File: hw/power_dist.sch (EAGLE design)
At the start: 83 parts, among them J1 JST-ZH6SMT_VERT, J2 JST-PH4SMT_VERT, J3 JST-PH5VERT, P1 XT30P, P2 XT30P, P3 XT30P, P4 XT30P, P5 XT30P, P6 XT30P, P7 XT90PW-M, Q1 PSMN4R8-100BSEJ, Q2 PSMN4R8-100BSEJ, Q3 PSMN4R8-100BSEJ, Q4 MF-DSC-SOT233-MMBT3904, Q5 MMBT5401 100V, U1 MAX15062AATA+T, U2 STM32G474CEU6, U3 TPS2490DGSR, U4 TCAN334G, U5 LT1787HVIMS8PBF

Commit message: Connect TIMER to an ADC and add a FET temperature sensor
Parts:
- added C21: 0.1uF, mfpassives:CAPACITOR_NP_0603
- added U6: STLM20DD9FUDFN-4L_STM-L, power_dist:STLM20DD9FUDFN-4L_STM-L
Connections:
- new net FET_TEMP: U2.PC4, U6.VOUT
- net GND: now also C21.P$2, U6.GND
- net TIMER: now also U2.PB11
- net VCC: now also C21.P$1, U6.VCC
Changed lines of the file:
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@@
 </part>
 <part name="GND7" library="supply1" deviceset="GND" device=""/>
+<part name="U6" library="power_dist" deviceset="STLM20DD9F" device="UDFN-4L_STM-L">
+<attribute name="MPN" value="STLM20DD9F"/>
+<attribute name="POPULATE" value="1"/>
+</part>
+<part name="P+8" library="supply1" deviceset="VCC" device=""/>
+<part name="GND9" library="supply1" deviceset="GND" device=""/>
+<part name="C21" library="mfpassives" deviceset="CAPACITOR_NP" device="_0603" value="0.1uF">
+<attribute name="HOUSEPART" value="1"/>
+<attribute name="MPN" value="MF-CAP-0603-0.1uF"/>
+</part>
 </parts>
 <sheets>
@@
 <attribute name="VALUE" x="-38.1" y="5.08" size="1.778" layer="96"/>
 </instance>
+<instance part="U6" gate="A" x="134.62" y="-66.04" smashed="yes">
+<attribute name="NAME" x="150.2156" y="-56.9214" size="2.0828" layer="95" ratio="6" rot="SR0"/>
+<attribute name="VALUE" x="149.5806" y="-59.4614" size="2.0828" layer="96" ratio="6" rot="SR0"/>
+<attribute name="MPN" x="134.62" y="-66.04" size="1.778" layer="96" display="off"/>
+<attribute name="POPULATE" x="134.62" y="-66.04" size="1.778" layer="96" display="off"/>
+</instance>
+<instance part="P+8" gate="VCC" x="180.34" y="-45.72" smashed="yes">
+<attribute name="VALUE" x="177.8" y="-48.26" size="1.778" layer="96" rot="R90"/>
+</instance>
+<instance part="GND9" gate="1" x="180.34" y="-83.82" smashed="yes">
+<attribute name="VALUE" x="177.8" y="-86.36" size="1.778" layer="96"/>
+</instance>
+<instance part="C21" gate="G$1" x="180.34" y="-68.58" smashed="yes">
+<attribute name="NAME" x="182.88" y="-67.056" size="1.016" layer="95" font="vector" align="top-left"/>
+<attribute name="VALUE" x="182.88" y="-70.104" size="1.016" layer="96" font="vector"/>
+</instance>
 </instances>
 <busses>
@@
 <pinref part="GND7" gate="1" pin="GND"/>
 <wire x1="-35.56" y1="12.7" x2="-35.56" y2="10.16" width="0.1524" layer="91"/>
+</segment>
+<segment>
+<pinref part="U6" gate="A" pin="GND"/>
+<wire x1="172.72" y1="-68.58" x2="172.72" y2="-71.12" width="0.1524" layer="91"/>
+<wire x1="172.72" y1="-71.12" x2="180.34" y2="-71.12" width="0.1524" layer="91"/>
+<wire x1="180.34" y1="-71.12" x2="180.34" y2="-81.28" width="0.1524" layer="91"/>
+<pinref part="GND9" gate="1" pin="GND"/>
+<pinref part="C21" gate="G$1" pin="P$2"/>
+<junction x="180.34" y="-71.12"/>
 </segment>
 </net>
@@
 <wire x1="208.28" y1="-20.32" x2="208.28" y2="-17.78" width="0.1524" layer="91"/>
 </segment>
+<segment>
+<pinref part="U6" gate="A" pin="VCC"/>
+<wire x1="172.72" y1="-66.04" x2="180.34" y2="-66.04" width="0.1524" layer="91"/>
+<wire x1="180.34" y1="-66.04" x2="180.34" y2="-48.26" width="0.1524" layer="91"/>
+<pinref part="P+8" gate="VCC" pin="VCC"/>
+<pinref part="C21" gate="G$1" pin="P$1"/>
+<junction x="180.34" y="-66.04"/>
+</segment>
 </net>
 <net name="NRST" class="0">
@@
 <label x="-17.78" y="-50.8" size="1.778" layer="95" rot="R90"/>
 </segment>
+<segment>
+<pinref part="U2" gate="G$1" pin="PB11"/>
+<wire x1="482.6" y1="106.68" x2="482.6" y2="104.14" width="0.1524" layer="91"/>
+<wire x1="482.6" y1="104.14" x2="510.54" y2="104.14" width="0.1524" layer="91"/>
+<label x="502.92" y="104.14" size="1.778" layer="95"/>
+</segment>
 </net>
 <net name="LTC_EN" class="0">
@@
 <wire x1="459.74" y1="106.68" x2="459.74" y2="96.52" width="0.1524" layer="91"/>
 <wire x1="459.74" y1="96.52" x2="441.96" y2="96.52" width="0.1524" layer="91"/>
-<label x="441.96" y="96.52" size="1.778" layer="95"/>
+<label x="436.88" y="96.52" size="1.778" layer="95"/>
 </segment>
 <segment>
@@
 </segment>
 </net>
+<net name="FET_TEMP" class="0">
+<segment>
+<pinref part="U6" gate="A" pin="VOUT"/>
+<wire x1="137.16" y1="-66.04" x2="124.46" y2="-66.04" width="0.1524" layer="91"/>
+<wire x1="124.46" y1="-66.04" x2="124.46" y2="-45.72" width="0.1524" layer="91"/>
+<label x="124.46" y="-50.8" size="1.778" layer="95"/>
+</segment>
+<segment>
+<pinref part="U2" gate="G$1" pin="PC4"/>
+<wire x1="462.28" y1="106.68" x2="462.28" y2="96.52" width="0.1524" layer="91"/>
+<label x="462.28" y="106.68" size="1.778" layer="95" rot="R270"/>
+</segment>
+</net>

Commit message: Renumber all resistors and caps
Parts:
- C16: value DNP -> 0.1uF; HOUSEPART (none) -> 1; MPN (none) -> MF-CAP-0603-0.1uF; POPULATE 0 -> (none)
- C17: value 0.01uF -> DNP; HOUSEPART 1 -> (none); MPN MF-CAP-0603-0.01uF -> (none); POPULATE (none) -> 0
- C19: value 0.1uF -> 0.01uF; MPN MF-CAP-0603-0.1uF -> MF-CAP-0603-0.01uF
- R10: value 3M 1% -> 220; MPN (none) -> MF-RES-0603-220
- R11, R13: value 200k 1% -> 3M 1%
- R12: value 3M 1% -> 200k 1%
- R14: value 220 -> 200k 1%; MPN MF-RES-0603-220 -> (none)
- R15: value 1k -> 220; MPN (none) -> MF-RES-0603-220
- R16: value 500k -> 1k
- R17: value 2M -> 500k
- R18: value 200k -> 2M
- R19: value 6.8k 1% -> 200k
- R4: value 47k 1% -> 0.5mOhm; device mfpassives:RESISTOR_0603 -> power_dist:SENSE_RESISTOR2512; HOUSEPART 1 -> (none); MF (none) -> VISHAY DALE; MPN (none) -> WSLF2512L5000FEA; POPULATE (none) -> 1
- R7: value 0.5mOhm -> 47k 1%; device power_dist:SENSE_RESISTOR2512 -> mfpassives:RESISTOR_0603; HOUSEPART (none) -> 1; MF VISHAY DALE -> (none); MPN WSLF2512L5000FEA -> (none); POPULATE 1 -> (none)
- R8: value 220 -> 6.8k 1%; MPN MF-RES-0603-220 -> (none)
- renumbered SH4 to SH1
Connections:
- net +24V: now also R11.P$2, R4.1; no longer R10.P$2, R7.1
- net GND: now also C16.P$2, R12.P$1, R14.P$1, R8.P$1; no longer C17.P$2, R11.P$1, R13.P$1, R18.P$1
- net ISAMP_BIAS: now also C20.P$1; no longer C19.P$1
- net N$11: now also R18.P$1; no longer R17.P$1
- net N$13: now also R19.P$2; no longer R18.P$2
- net N$14: now also R10.P$1; no longer R9.P$1
- net N$17: now also R17.P$1; no longer R16.P$1
- net N$18: now also R16.P$1; no longer R15.P$1
- net N$2: now also R15.P$1; no longer R14.P$1
- net N$6: now also C17.P$1; no longer C16.P$1
- net N$7: now also C17.P$2; no longer C16.P$2
- net N$8: now also R9.P$1; no longer R8.P$1
- net PROG: now also R7.P$1, R8.P$2; no longer R19.P$2, R4.P$1
- net PWR_LED: now also R15.P$2; no longer R14.P$2
- net PWR_OVERRIDE: now also R16.P$2; no longer R15.P$2
- net PWR_SW: now also R18.P$2; no longer R16.P$2
- net VCC: now also C16.P$1, R10.P$2; no longer C20.P$1, R8.P$2
- net VIN_SAMP: now also C18.P$1, R11.P$1, R12.P$2; no longer C17.P$1, R10.P$1, R11.P$2
- net VREF: now also R7.P$2; no longer R4.P$2
- net VSENSE: now also R4.2; no longer R7.2
- net VSENSE_HIGH: now also R4.S1; no longer R7.S1
- net VSENSE_LOW: now also R4.S2; no longer R7.S2
- net VSWITCHED: now also R13.P$2; no longer R12.P$2
- net VSWITCHED_SAMP: now also C19.P$1, R13.P$1, R14.P$2; no longer C18.P$1, R12.P$1, R13.P$2
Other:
- note added: "This circuit exists to keep the TPS disabled until the switch is closed, but also to draw minimal quiescent current both while it is disabled, and while the switch is closed and the TPS controller is enabled. Also, it supports the microcontroller latching the TPS on, while still being able to monitor the state of the actual power switch."
- note removed: "This circuit exists to keep the LTC disabled until the switch is closed, but also to draw minimal quiescent current both while it is disabled, and while the switch is closed and the LTC controller is enabled. Also, it supports the microcontroller latching the LTC on, while still being able to monitor the state of the actual power switch."
- moved on the sheet: C16, C17, C18, C19, C20, C21, R10, R11, R12, R13, R14, R15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

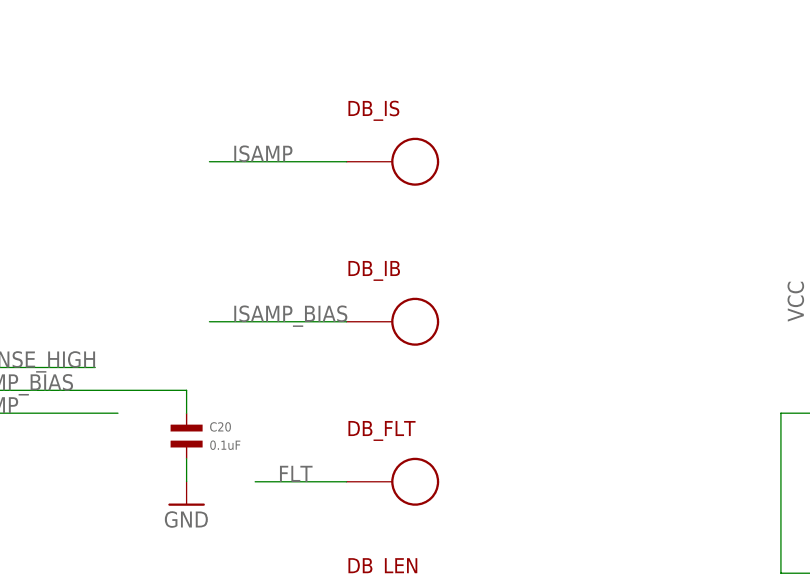
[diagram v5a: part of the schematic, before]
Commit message: Place all silks and add a few more debug points
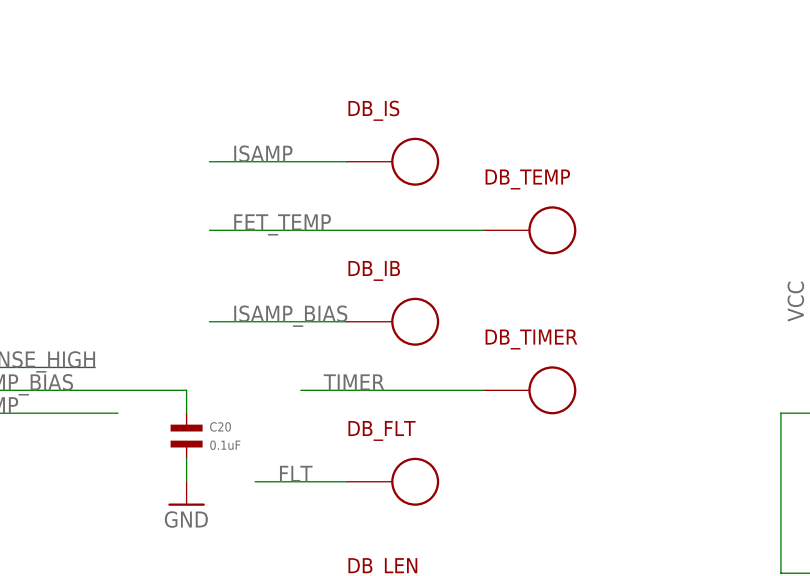
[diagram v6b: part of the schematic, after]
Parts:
- added DB_TEMP, DB_TIMER: PAD24AWG_PAD, precharge:PAD24AWG_PAD
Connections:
- net FET_TEMP: now also DB_TEMP.P$1
- net TIMER: now also DB_TIMER.P$1
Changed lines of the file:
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@@
 <attribute name="MPN" value="MF-CAP-0603-0.1uF"/>
+</part>
+<part name="DB_TEMP" library="precharge" deviceset="PAD" device="24AWG_PAD">
+<attribute name="POPULATE" value="0"/>
+</part>
+<part name="DB_TIMER" library="precharge" deviceset="PAD" device="24AWG_PAD">
+<attribute name="POPULATE" value="0"/>
 </part>
 </parts>
@@
 <attribute name="VALUE" x="182.88" y="-70.104" size="1.016" layer="96" font="vector"/>
 </instance>
+<instance part="DB_TEMP" gate="G$1" x="337.82" y="35.56" smashed="yes">
+<attribute name="POPULATE" x="337.82" y="35.56" size="1.778" layer="96" font="vector" display="off"/>
+<attribute name="NAME" x="330.2" y="40.64" size="1.6764" layer="94"/>
+</instance>
+<instance part="DB_TIMER" gate="G$1" x="337.82" y="17.78" smashed="yes">
+<attribute name="POPULATE" x="337.82" y="17.78" size="1.778" layer="96" font="vector" display="off"/>
+<attribute name="NAME" x="330.2" y="22.86" size="1.6764" layer="94"/>
+</instance>
 </instances>
 <busses>
@@
 <label x="502.92" y="104.14" size="1.778" layer="95"/>
 </segment>
+<segment>
+<pinref part="DB_TIMER" gate="G$1" pin="P$1"/>
+<wire x1="330.2" y1="17.78" x2="309.88" y2="17.78" width="0.1524" layer="91"/>
+<label x="312.42" y="17.78" size="1.778" layer="95"/>
+</segment>
 </net>
 <net name="LTC_EN" class="0">
@@
 <label x="462.28" y="106.68" size="1.778" layer="95" rot="R270"/>
 </segment>
-</net>
+<segment>
+<pinref part="DB_TEMP" gate="G$1" pin="P$1"/>
+<wire x1="330.2" y1="35.56" x2="299.72" y2="35.56" width="0.1524" layer="91"/>
+<label x="302.26" y="35.56" size="1.778" layer="95"/>
+</segment>
+</net>

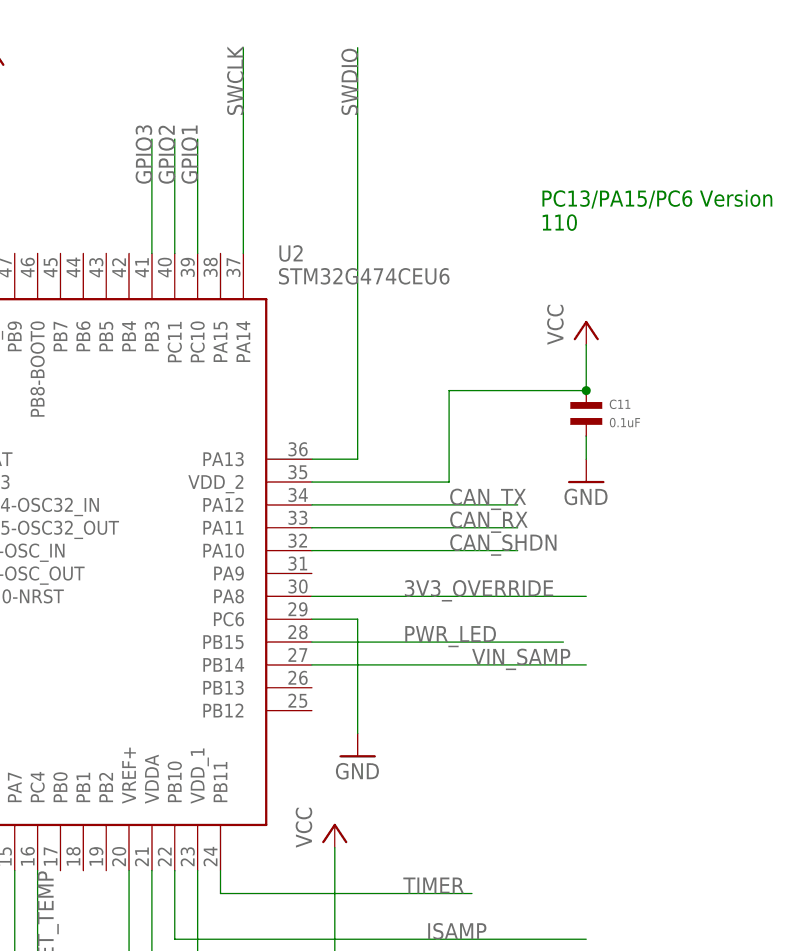
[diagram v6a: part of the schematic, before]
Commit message: Update version pins for r4.2
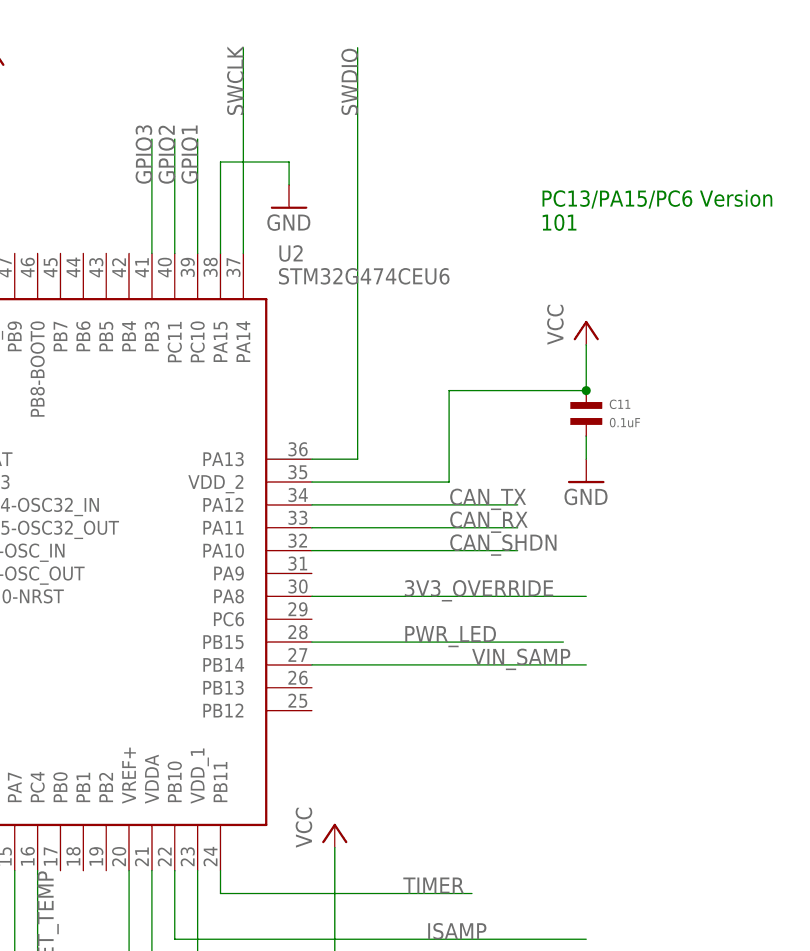
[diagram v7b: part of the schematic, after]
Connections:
- net GND: now also U2.PA15; no longer U2.PC6
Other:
- note added: "PC13/PA15/PC6 Version 101"
- note removed: "PC13/PA15/PC6 Version 110"
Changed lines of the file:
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@@
 <part name="GND14" library="supply1" deviceset="GND" device=""/>
 <part name="P+9" library="supply1" deviceset="VCC" device=""/>
-<part name="GND23" library="supply1" deviceset="GND" device=""/>
 <part name="DB_G" library="precharge" deviceset="PAD" device="24AWG_PAD">
 <attribute name="POPULATE" value="0"/>
@@
 <attribute name="POPULATE" value="0"/>
 </part>
+<part name="GND27" library="supply1" deviceset="GND" device=""/>
 </parts>
 <sheets>
@@
 <text x="358.14" y="40.64" size="7.62" layer="90" font="vector">INTERFACE</text>
 <text x="518.16" y="177.8" size="1.778" layer="91">PC13/PA15/PC6 Version
-110</text>
+101</text>
 <text x="500.38" y="40.64" size="1.778" layer="100" align="top-left">This circuit exists to keep the TPS
 disabled until the switch is closed,
@@
 <attribute name="VALUE" x="162.56" y="15.24" size="1.778" layer="96" rot="R90"/>
 </instance>
-<instance part="GND23" gate="1" x="497.84" y="119.38" smashed="yes">
-<attribute name="VALUE" x="495.3" y="116.84" size="1.778" layer="96"/>
-</instance>
 <instance part="DB_G" gate="G$1" x="322.58" y="-68.58" smashed="yes">
 <attribute name="POPULATE" x="322.58" y="-68.58" size="1.778" layer="96" font="vector" display="off"/>
@@
 <attribute name="POPULATE" x="337.82" y="17.78" size="1.778" layer="96" font="vector" display="off"/>
 <attribute name="NAME" x="330.2" y="22.86" size="1.6764" layer="94"/>
+</instance>
+<instance part="GND27" gate="1" x="490.22" y="180.34" smashed="yes">
+<attribute name="VALUE" x="487.68" y="177.8" size="1.778" layer="96"/>
 </instance>
 </instances>
@@
 </segment>
 <segment>
-<pinref part="U2" gate="G$1" pin="PC6"/>
-<wire x1="492.76" y1="134.62" x2="497.84" y2="134.62" width="0.1524" layer="91"/>
-<pinref part="GND23" gate="1" pin="GND"/>
-<wire x1="497.84" y1="134.62" x2="497.84" y2="121.92" width="0.1524" layer="91"/>
-</segment>
-<segment>
 <pinref part="DB_G" gate="G$1" pin="P$1"/>
 <wire x1="314.96" y1="-68.58" x2="312.42" y2="-68.58" width="0.1524" layer="91"/>
@@
 <junction x="180.34" y="-71.12"/>
 </segment>
+<segment>
+<pinref part="U2" gate="G$1" pin="PA15"/>
+<wire x1="482.6" y1="175.26" x2="482.6" y2="185.42" width="0.1524" layer="91"/>
+<wire x1="482.6" y1="185.42" x2="490.22" y2="185.42" width="0.1524" layer="91"/>
+<pinref part="GND27" gate="1" pin="GND"/>
+<wire x1="490.22" y1="185.42" x2="490.22" y2="182.88" width="0.1524" layer="91"/>
+</segment>
 </net>

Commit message: Incorporate r4.1 feedback
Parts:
- added C22, C23: DNP, mfpassives:CAPACITOR_NP_0603
- added DB_IAMP, DB_IBUF: PAD24AWG_PAD, precharge:PAD24AWG_PAD
- added R20: 100k, mfpassives:RESISTOR_0603
- added R21, R23: 33k, mfpassives:RESISTOR_0603
- added R22, R25: DNP, mfpassives:RESISTOR_0603
- added R24, R26: 0, mfpassives:RESISTOR_0603
- R2: value DNP -> 100k
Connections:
- new net ISAMP_AMP: DB_IAMP.P$1, U2.PA8
- new net ISAMP_BUF: DB_IBUF.P$1, U2.PB1, U2.PB15
- new net N$10: R26.P$1, U2.PA1
- new net N$3: R24.P$2, U5.VBIAS
- new net N$5: C23.P$1, U2.PA3
- net 3V3_OVERRIDE: now also U2.PB13; no longer U2.PA8
- net FLT: now also R21.P$1
- net GND: now also C23.P$2, R20.P$1, R22.P$1
- net ISAMP: now also C22.P$2, R25.P$2, U2.PB0; no longer U2.PB10
- net ISAMP_BIAS: now also C22.P$1, R24.P$1, R25.P$1, R26.P$2; no longer U5.VBIAS
- net LED2: now also U2.PB9; no longer U2.PA1
- net N$11: now also R22.P$2
- net PWR_LED: now also U2.PB12; no longer U2.PB15
- net PWR_OVERRIDE: now also U2.PC14-OSC32_IN; no longer U2.PA3
- net PWR_SW: now also D2.ANODE, R20.P$2
- net SNS_PWR_SW: now also R23.P$1
- net VCC: now also R21.P$2, R23.P$2
- net VSWITCHED: no longer D2.ANODE
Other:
- moved on the sheet: C20, C5
